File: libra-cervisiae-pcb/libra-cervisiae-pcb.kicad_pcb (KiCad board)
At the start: 2 copper layers, 63.8 x 43.2 mm, 130 parts, among them CN1 CP2102-BREAKOUT, CN2 HX711_BREAKOUT, J1 Wort Temp, J2 Ambient Temp, J3 Load Cells, SW1 Reset, SW2 Flash, U1 ESP-12F, U2 VREG

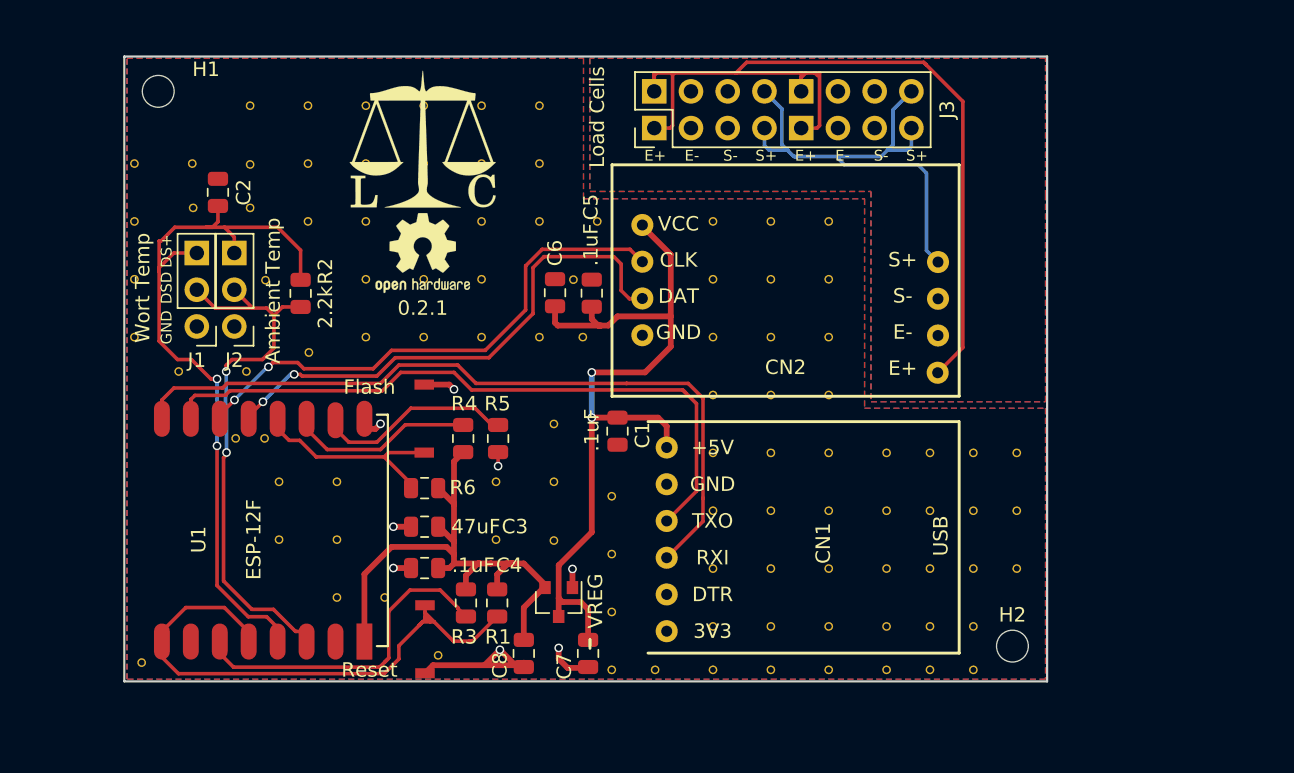
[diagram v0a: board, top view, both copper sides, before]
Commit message: Schematic and layout for ESP32 version
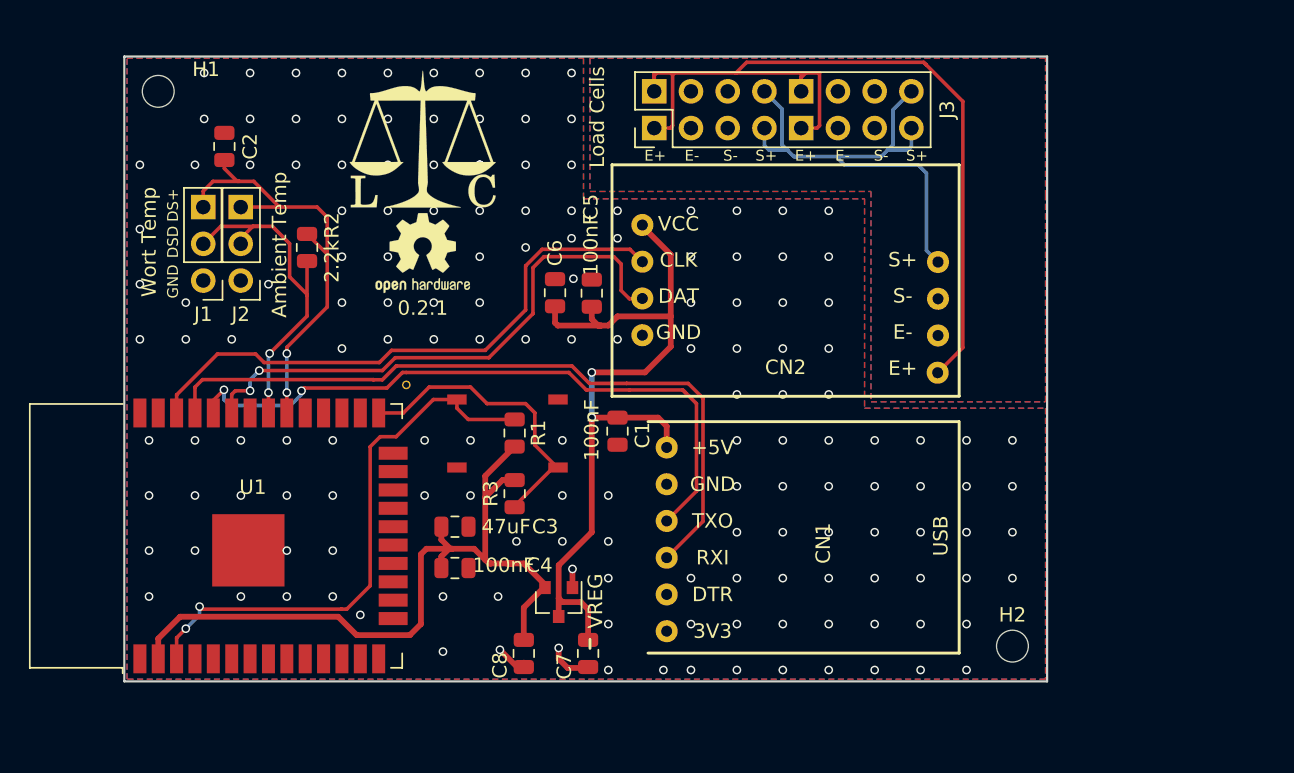
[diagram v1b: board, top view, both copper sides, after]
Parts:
- removed R4, R5, R6: 10k, Resistor_SMD:R_0805_2012Metric
- removed the REF** at (111.0, 76.0)
- removed the REF** at (139.9, 107.9)
- removed the REF** at (146.9, 96.9)
- removed the REF** at (150.9, 96.9)
- removed the REF** at (154.9, 96.9)
- removed the REF** at (158.9, 96.9)
- removed the REF** at (139.9, 103.9)
- removed the REF** at (139.9, 99.9)
- removed the REF** at (139.9, 95.9)
- removed the REF** at (164.9, 107.9)
- removed the REF** at (161.9, 107.9)
- removed the REF** at (161.9, 104.9)
- removed the REF** at (164.9, 104.9)
- removed the REF** at (164.9, 100.9)
- removed the REF** at (161.9, 100.9)
- removed the REF** at (114.9, 76.0)
- removed the REF** at (161.9, 96.9)
- removed the REF** at (164.9, 96.9)
- removed the REF** at (164.9, 92.9)
- removed the REF** at (154.9, 84.9)
- removed the REF** at (154.9, 80.9)
- removed the REF** at (154.9, 76.9)
- removed the REF** at (150.9, 84.9)
- removed the REF** at (150.9, 80.9)
- removed the REF** at (150.9, 76.9)
- removed the REF** at (146.9, 88.9)
- removed the REF** at (114.9, 73.0)
- removed the REF** at (146.9, 84.9)
- removed the REF** at (146.9, 80.9)
- removed the REF** at (146.9, 76.9)
- removed the REF** at (138.9, 76.9)
- removed the REF** at (134.9, 76.9)
- removed the REF** at (134.9, 72.9)
- removed the REF** at (106.9, 84.9)
- removed the REF** at (106.9, 80.9)
- removed the REF** at (106.9, 76.9)
- removed the REF** at (106.9, 72.9)
- removed the REF** at (110.0, 87.3)
- removed the REF** at (110.9, 72.9)
- removed the REF** at (118.9, 72.9)
- removed the REF** at (118.9, 76.9)
- removed the REF** at (114.9, 68.9)
- removed the REF** at (137.3, 81.0)
- removed the REF** at (137.9, 84.9)
- removed the REF** at (134.9, 68.9)
- removed the REF** at (134.9, 84.9)
- removed the REF** at (130.9, 84.9)
- removed the REF** at (161.9, 92.9)
- removed the REF** at (116.0, 81.0)
- removed the REF** at (167.9, 96.9)
- removed the REF** at (131.9, 94.9)
- removed the REF** at (124.2, 102.9)
- removed the REF** at (135.9, 94.9)
- removed the REF** at (135.9, 90.9)
- removed the REF** at (120.9, 102.9)
- removed the REF** at (120.9, 98.9)
- removed the REF** at (120.9, 94.9)
- removed the REF** at (116.9, 94.9)
- removed the REF** at (116.9, 98.9)
- removed the REF** at (119.0, 86.0)
- removed the REF** at (107.4, 107.4)
- removed the REF** at (115.9, 91.9)
- removed the REF** at (113.9, 91.9)
- removed the REF** at (130.9, 80.9)
- removed the REF** at (130.9, 76.9)
- removed the REF** at (130.9, 72.9)
- removed the REF** at (130.9, 68.9)
- removed the REF** at (118.9, 68.9)
- removed the REF** at (126.9, 68.9)
- removed the REF** at (122.9, 68.9)
- removed the REF** at (114.7, 87.3)
- removed the REF** at (122.9, 72.9)
- removed the REF** at (126.9, 72.9)
- removed the REF** at (126.9, 76.9)
- removed the REF** at (122.9, 76.9)
- removed the REF** at (122.9, 80.9)
- removed the REF** at (126.9, 80.9)
- removed the REF** at (126.9, 84.9)
- removed the REF** at (122.9, 84.9)
- removed the REF** at (131.9, 98.9)
- removed the REF** at (127.9, 106.9)
- removed the REF** at (135.9, 99.0)
- removed the REF** at (150.9, 88.9)
- removed the REF** at (154.9, 88.9)
- removed the REF** at (167.9, 92.9)
- removed the REF** at (167.9, 100.9)
- removed the REF** at (158.9, 107.9)
- removed the REF** at (154.9, 107.9)
- removed the REF** at (150.9, 107.9)
- removed the REF** at (146.9, 107.9)
- removed the REF** at (146.9, 104.9)
- removed the REF** at (146.9, 100.9)
- removed the REF** at (142.9, 107.9)
- removed the REF** at (150.9, 100.9)
- removed the REF** at (154.9, 100.9)
- removed the REF** at (150.9, 104.9)
- removed the REF** at (154.9, 104.9)
- removed the REF** at (158.9, 104.9)
- removed the REF** at (158.9, 100.9)
- removed the REF** at (158.9, 92.9)
- removed the REF** at (154.9, 92.9)
- removed the REF** at (150.9, 92.9)
- removed the REF** at (146.9, 92.9)
- added REF**: Stitch, Extra_Pads:Stitching_Via_0.6mm, F.Cu at (125.7, 88.2)
- C1, C4, C5: value .1uF -> 100nF
- U1: value ESP-12F -> ESP32-WROOM-32; footprint ESP8266:ESP-12E -> RF_Module:ESP32-WROOM-32
- moved SW1 14.4 mm to (127.6, 88.9)
- moved R1 11.8 mm to (133.2, 91.6)
- moved U1 9.43 mm to (115.6, 98.7)
- moved R3 8.27 mm to (133.2, 95.8)
- moved SW2 7.46 mm to (134.6, 88.9), turned to 0 degrees
- moved R2 3.21 mm to (118.9, 78.7)
- moved C2 3.21 mm to (113.2, 71.8)
- moved J1 3.21 mm to (111.7, 81.0)
- moved J2 3.21 mm to (114.3, 81.0)
- moved C3 2.10 mm to (129.1, 98.0)
- moved C4 2.10 mm to (129.1, 100.9)
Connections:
- C3 pad 1: /3.3+ -> /GND
- C3 pad 2: /GND -> /3.3+
- C4 pad 1: /3.3+ -> /GND
- C4 pad 2: /GND -> /3.3+
- R1 pad 1: /3.3+ -> Net-(R1-Pad1)
- R1 pad 2: /RST -> /3.3+
- SW1 pad 1: /RST -> Net-(R1-Pad1)
- SW2 pad 1: /FLASH -> /GND
- SW2 pad 2: /GND -> Net-(R3-Pad1)
- U1 pad 1: /RST -> /GND
- U1 pad 10: Net-(R5-Pad2) -> (no net)
- U1 pad 11: Net-(R4-Pad2) -> (no net)
- U1 pad 12: /FLASH -> (no net)
- U1 pad 13: /DAT -> (no net)
- U1 pad 14: /CLK -> (no net)
- U1 pad 15: /HostTX -> /GND
- U1 pad 16: /HostRX -> (no net)
- U1 pad 2: (no net) -> /3.3+
- U1 pad 3: Net-(R3-Pad1) -> Net-(R1-Pad1)
- U1 pad 4: /RST -> (no net)
- U1 pad 5: /DS+ -> (no net)
- U1 pad 6: /DSD -> (no net)
- U1 pad 8: /3.3+ -> (no net)
- U1 pad 9: /GND -> (no net)
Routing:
- net /RST: track 39.1 -> 0.00 mm
- net Net-(R1-Pad1): track 0.00 -> 38.7 mm, vias 0 -> 2
- net /DS+: track 52.2 -> 32.6 mm
- net /3.3+: track 39.9 -> 55.3 mm
- net /GND: track 22.1 -> 7.01 mm, vias 8 -> 163
- net /DSD: track 39.2 -> 24.7 mm
- net Net-(R5-Pad2): track 14.2 -> 0.00 mm
- net /FLASH: track 14.0 -> 0.00 mm
- net Net-(R4-Pad2): track 12.5 -> 0.00 mm
- net Net-(R3-Pad1): track 24.1 -> 20.9 mm
- net /HostRX: track 53.4 -> 50.5 mm
- net /CLK: track 37.5 -> 40.2 mm, vias 2 -> 0
- net /HostTX: track 49.3 -> 46.5 mm, vias 0 -> 2

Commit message: Fatten load cell traces
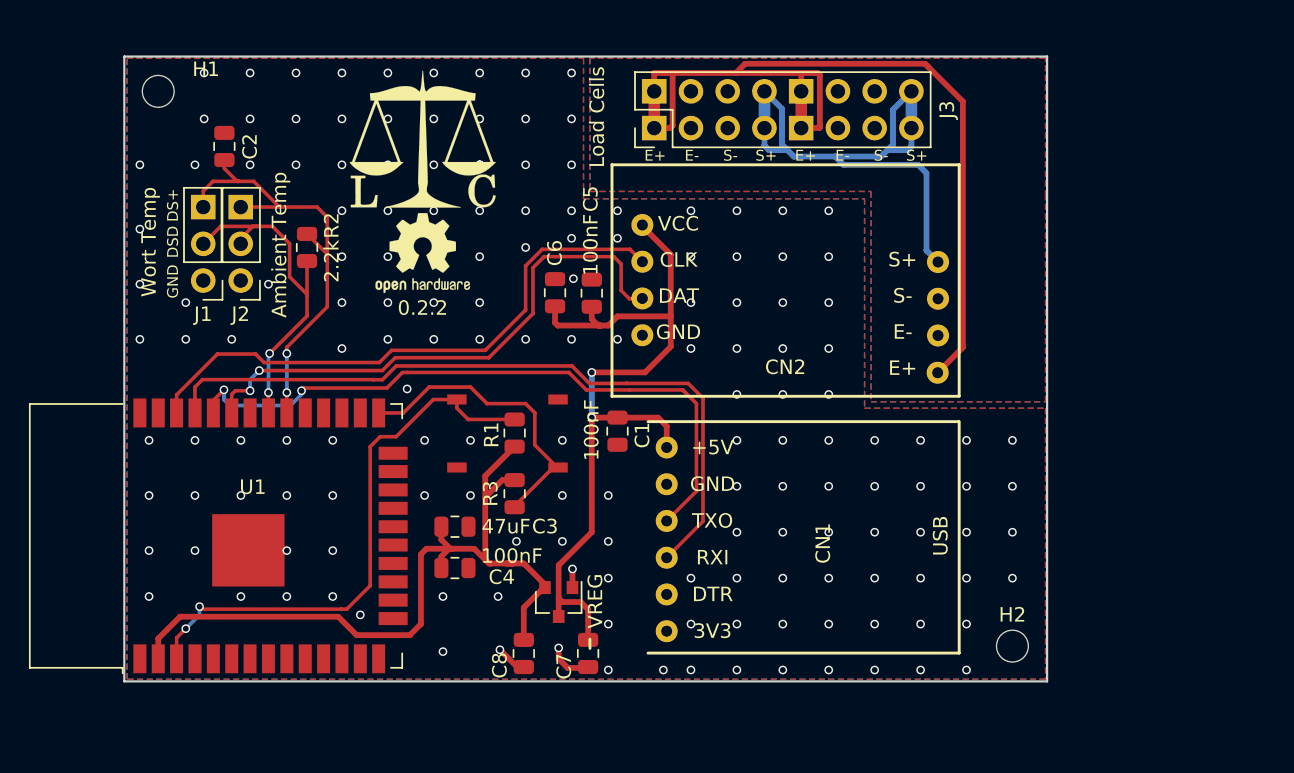
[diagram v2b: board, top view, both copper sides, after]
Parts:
- removed REF**: Stitch, Extra_Pads:Stitching_Via_0.6mm
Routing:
- net /S+: track 36.1 -> 44.2 mm
- net /E+: track 62.5 -> 66.9 mm
- net /GND: vias 163 -> 164
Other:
- board text added: "0.2.2"
- board text removed: "0.2.1"

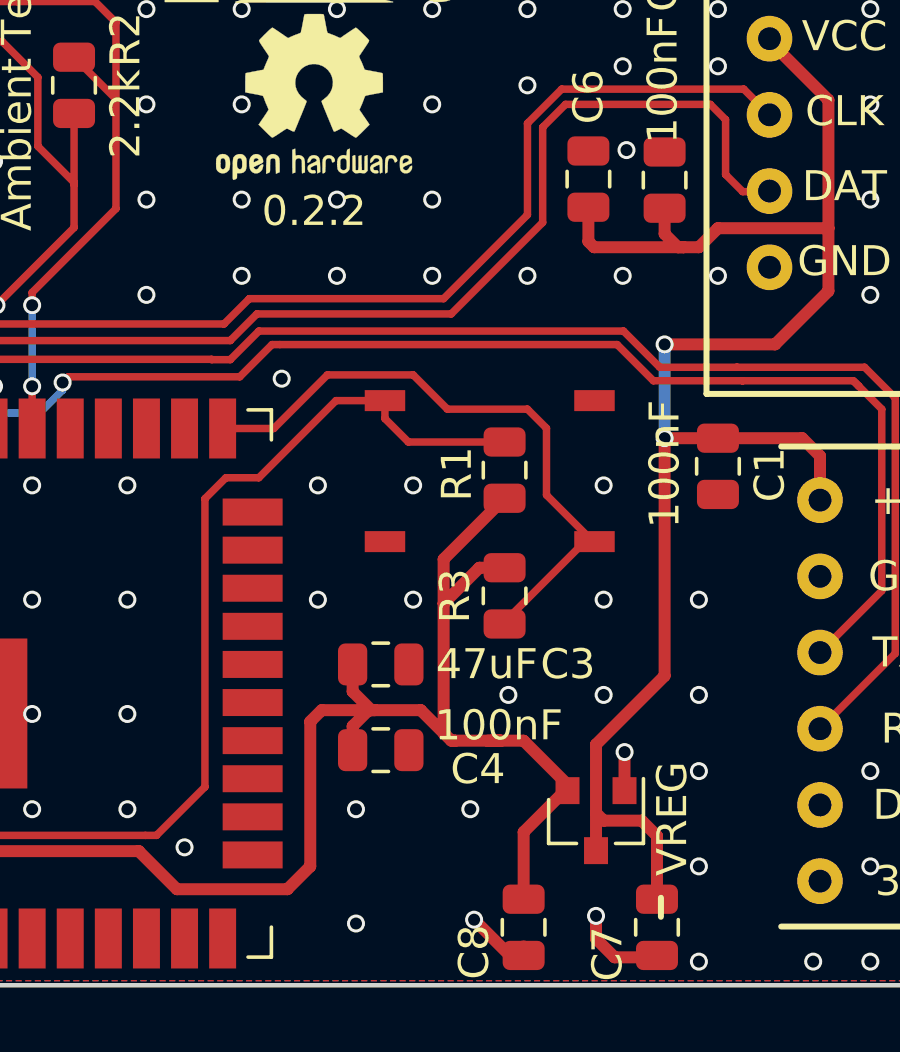
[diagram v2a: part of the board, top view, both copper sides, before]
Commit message: 0.3.0 schematic/layout
1. Bump board capacitance down for USB inrush current reasons
The previous 47uF capacitor on the board worked on one of my PCs
but not the other. Swap it for a 4.7uF cap, which sneaks us in
just under the 10uF limit the USB spec requires.

2. Version numbers up
The ESP32 change is significant enough to warrant it.
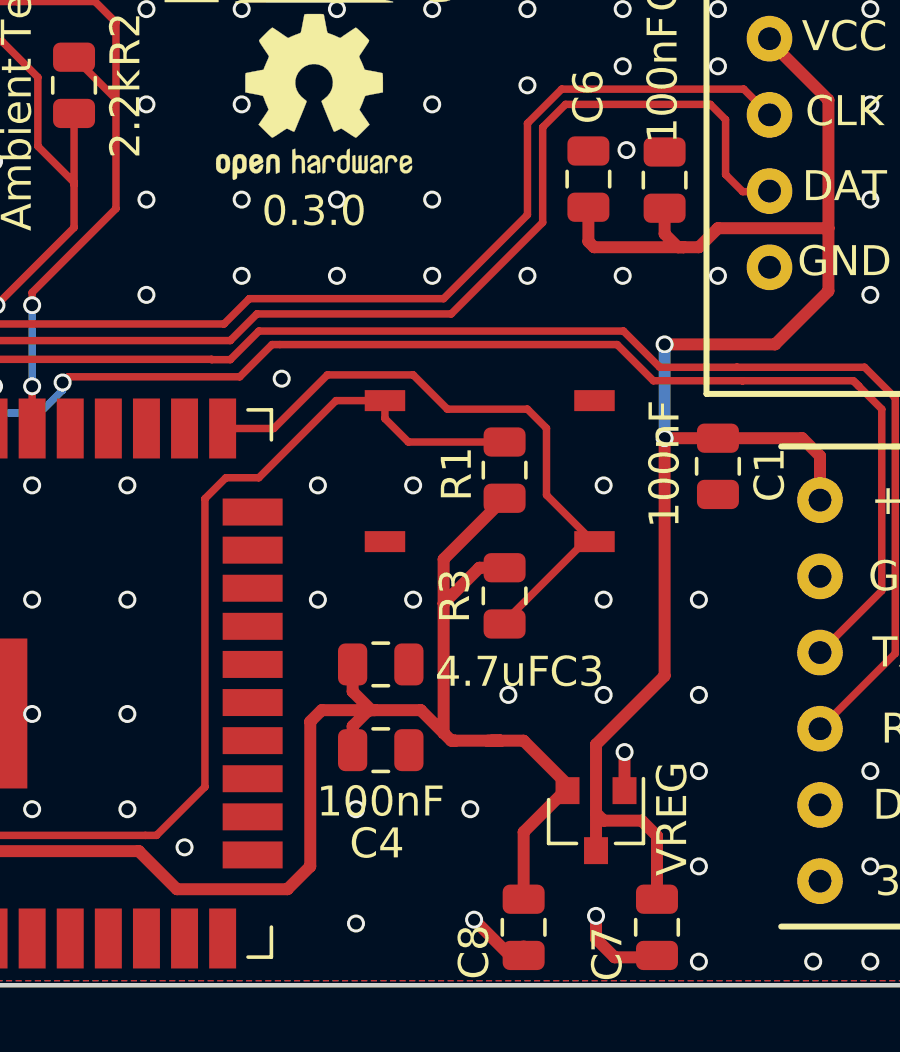
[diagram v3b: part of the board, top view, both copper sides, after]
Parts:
- C3: value 47uF -> 4.7uF
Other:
- board text added: "0.3.0"
- board text removed: "0.2.2"
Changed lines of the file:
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@@
   (general
     (thickness 1.6)
-    (drawings 28)
+    (drawings 27)
     (tracks 428)
     (zones 0)
@@
   (title_block
     (title "Libra Cervisiae PCB")
-    (date 2018-08-30)
-    (rev 0.2.0)
+    (date 2019-08-16)
+    (rev 0.3.0)
   )
   (layers
@@
   )
   (setup
-    (last_trace_width 0.4)
+    (last_trace_width 0.25)
     (user_trace_width 0.4)
     (user_trace_width 0.8)
@@
     (tags capacitor)
     (attr smd)
-    (fp_text reference C3 (at -6.238 0.006 180) (layer F.SilkS)
-      (effects (font (size 1 1) (thickness 0.15)))
-    )
-    (fp_text value 47uF (at -3.538 0.006 180) (layer F.SilkS)
+    (fp_text reference C3 (at -6.5405 -0.248 180) (layer F.SilkS)
+      (effects (font (size 1 1) (thickness 0.15)))
+    )
+    (fp_text value 4.7uF (at -3.7285 -0.248 180) (layer F.SilkS)
       (effects (font (size 1 1) (thickness 0.15)))
     )
@@
     (tags capacitor)
     (attr smd)
-    (fp_text reference C4 (at -3.2385 -0.635 180) (layer F.SilkS)
-      (effects (font (size 1 1) (thickness 0.15)))
-    )
-    (fp_text value 100nF (at -3.937 0.8255 180) (layer F.SilkS)
+    (fp_text reference C4 (at 0.127 -3.1115 180) (layer F.SilkS)
+      (effects (font (size 1 1) (thickness 0.15)))
+    )
+    (fp_text value 100nF (at 0 -1.7145 180) (layer F.SilkS)
       (effects (font (size 1 1) (thickness 0.15)))
     )
@@
     (arrow2b (pts (xy 100.138 111.738) (xy 101.264504 111.151579)))
   )
-  (gr_text 0.2.2 (at 126.873 82.931) (layer F.SilkS)
+  (gr_text 0.3.0 (at 126.873 82.931) (layer F.SilkS)
     (effects (font (size 1 1) (thickness 0.15)))
   )
-  (gr_line (start 138.434 105.821) (end 138.434 106.456) (angle 90) (layer F.SilkS) (width 0.2))
   (segment (start 135.321 102.251) (end 135.239 102.251) (width 0.4) (layer F.Cu) (net 1) (status 30))
   (segment (start 135.239 102.251) (end 133.858 103.632) (width 0.4) (layer F.Cu) (net 1) (status 10))
